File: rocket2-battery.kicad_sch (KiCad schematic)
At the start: 1 part

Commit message: Basic schematic
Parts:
- added C1: 1uF, symbol Device:C_Small
- added C2: 10uF, symbol Device:C_Small
- added C3: 0.1uF, symbol Device:C_Small
- added D1: BLUE_LED, symbol Device:LED_Small
- added D2: RED_LED, symbol Device:LED_Small
- added JP1: NO_Jump, symbol Jumper:Jumper_2_Open
- added Q1: DMG6968UDM-7, Package_TO_SOT_SMD:SOT-23-6, symbol Transistor_FET:DMG9926UDM
- added R1: 10k, symbol Device:R_Small
- added R2, R3, R9: 330, symbol Device:R_Small
- added R4: 27k, symbol Device:R_Small
- added R5: 375, symbol Device:R_Small
- added R6, R7: 100, symbol Device:R_Small
- added R8: 2.2k, symbol Device:R_Small
- added U2: BQ2970, Package_SON:WSON-6_1.5x1.5mm_P0.5mm, symbol Battery_Management:BQ297xy
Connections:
- net +5V: now reaches U1.1 (IN)
- net +5V: now also C1.1, C2.1, R2.2, R3.1
- net at U1.2 (ISET): now also R5.1
- net at U1.3 (TS): now also JP1.2 (B), R1.1
- net GND: now reaches U1.4 (GND)
- net GND: now also U1.9 (GND), C1.2, C2.2, C3.2, JP1.1 (A), Q1.3 (S2), R1.2, R4.2, R5.2, R8.1, U2.4 (VSS)
- net at U1.5 (STATUS): now also D1.1 (K)
- net at U1.6 (~{PG}): now also D2.1 (K)
- net at U1.7 (VSET): now also R4.1
- net BAT+: now reaches U1.8 (OUT)
- net BAT+: now also R9.1
- new net: Q1.2 (S1/D2), Q1.5 (S1/D2)
- new net: Q1.4 (G2), R6.1
- new net: Q1.6 (G1), R7.1
- new net: R7.2, U2.3 (Dout)
- new net: D2.2 (A), R2.1
- new net: R6.2, U2.2 (Cout)
- new net: D1.2 (A), R3.2
- new net: C3.1, R9.2, U2.5 (BAT)
- new net: R8.2, U2.6 (V-)
- new net BAT-: Q1.1 (D1)
- no-connect marks 0 -> 1
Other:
- note added: "DNP"

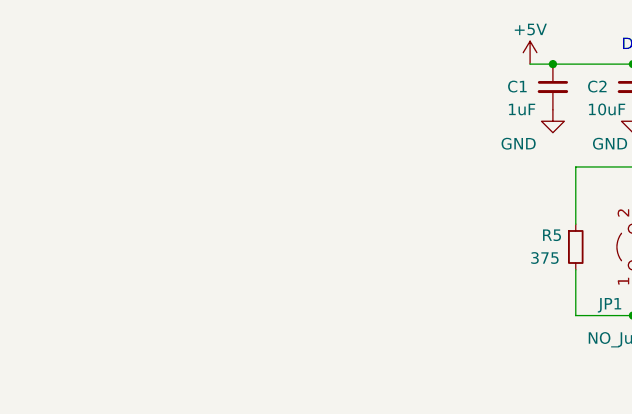
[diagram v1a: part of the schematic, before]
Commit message: added isolated 5v
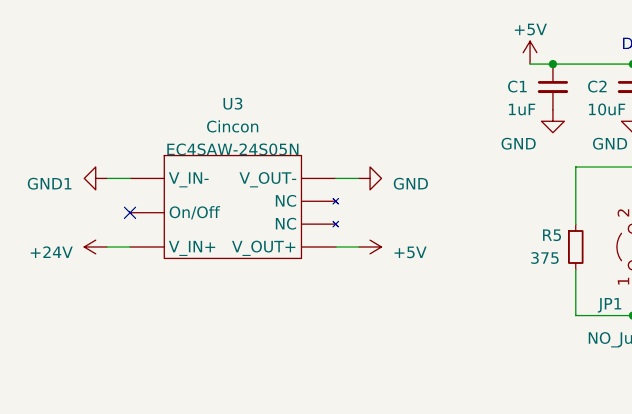
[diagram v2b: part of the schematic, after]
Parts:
- added U3: ~, symbol UCIRP-KiCAD-Lib:EC4SAW
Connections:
- net +5V: now also U3.6 (V_OUT+)
- net GND: now also U3.7 (V_OUT-)
- new net +24V: U3.2 (V_IN+)
- new net GND1: U3.1 (V_IN-)
- no-connect marks 1 -> 2
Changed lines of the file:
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@@
   )
   (no_connect (at 179.07 106.68))
+  (no_connect (at 54.61 92.71))
   (wire (pts (xy 200.66 80.01) (xy 205.74 80.01))
     (stroke (width 0) (type default))
@@
     (stroke (width 0) (type default))
   )
+  (wire (pts (xy 52.07 96.52) (xy 54.61 96.52))
+    (stroke (width 0) (type default))
+  )
   (wire (pts (xy 210.82 90.17) (xy 213.36 90.17))
     (stroke (width 0) (type default))
@@
     (stroke (width 0) (type default))
   )
+  (wire (pts (xy 52.07 88.9) (xy 54.61 88.9))
+    (stroke (width 0) (type default))
+  )
   (wire (pts (xy 130.81 104.14) (xy 165.1 104.14))
     (stroke (width 0) (type default))
@@
     (stroke (width 0) (type default))
   )
+  (wire (pts (xy 77.47 88.9) (xy 80.01 88.9))
+    (stroke (width 0) (type default))
+  )
   (wire (pts (xy 165.1 87.63) (xy 165.1 93.98))
     (stroke (width 0) (type default))
@@
   )
   (wire (pts (xy 213.36 80.01) (xy 213.36 90.17))
+    (stroke (width 0) (type default))
+  )
+  (wire (pts (xy 77.47 96.52) (xy 80.01 96.52))
     (stroke (width 0) (type default))
   )
@@
     )
   )
+  (symbol (lib_id "UCIRP-KiCAD-Lib:EC4SAW") (at 66.04 92.075 0) (unit 1)
+    (in_bom yes) (on_board yes) (dnp no) (fields_autoplaced)
+    (property "Reference" "U3" (at 66.04 80.645 0)
+      (effects (font (size 1.27 1.27)))
+    )
+    (property "Value" "~" (at 66.04 92.71 0)
+      (effects (font (size 1.27 1.27)))
+    )
+    (property "Footprint" "" (at 66.04 92.71 0)
+      (effects (font (size 1.27 1.27)) hide)
+    )
+    (property "Datasheet" "https://www.cincon.com/productdownload/Datasheet-EC4SAW-series.pdf" (at 66.04 92.71 0)
+      (effects (font (size 1.27 1.27)) hide)
+    )
+    (property "Manufacturer" "Cincon" (at 66.04 83.185 0)
+      (effects (font (size 1.27 1.27)))
+    )
+    (property "Part #" "EC4SAW-24S05N" (at 66.04 85.725 0)
+      (effects (font (size 1.27 1.27)))
+    )
+    (pin "1")
+    (pin "2")
+    (pin "3")
+    (pin "5")
+    (pin "6")
+    (pin "7")
+    (pin "8")
+    (instances
+      (project "rocket2-battery"
+        (path "/453543af-7e3c-49a0-a644-4bd49c4f86f8"
+          (reference "U3") (unit 1)
+        )
+      )
+    )
+  )
   (symbol (lib_id "Device:LED_Small") (at 147.32 95.25 270) (unit 1)
     (in_bom yes) (on_board yes) (dnp no)
@@
         (path "/453543af-7e3c-49a0-a644-4bd49c4f86f8"
           (reference "R6") (unit 1)
+        )
+      )
+    )
+  )
+  (symbol (lib_id "power:GND") (at 80.01 88.9 90) (unit 1)
+    (in_bom yes) (on_board yes) (dnp no) (fields_autoplaced)
+    (property "Reference" "#PWR010" (at 86.36 88.9 0)
+      (effects (font (size 1.27 1.27)) hide)
+    )
+    (property "Value" "GND" (at 83.82 89.535 90)
+      (effects (font (size 1.27 1.27)) (justify right))
+    )
+    (property "Footprint" "" (at 80.01 88.9 0)
+      (effects (font (size 1.27 1.27)) hide)
+    )
+    (property "Datasheet" "" (at 80.01 88.9 0)
+      (effects (font (size 1.27 1.27)) hide)
+    )
+    (pin "1")
+    (instances
+      (project "rocket2-battery"
+        (path "/453543af-7e3c-49a0-a644-4bd49c4f86f8"
+          (reference "#PWR010") (unit 1)
         )
       )
@@
     )
   )
+  (symbol (lib_id "power:+24V") (at 52.07 96.52 90) (unit 1)
+    (in_bom yes) (on_board yes) (dnp no) (fields_autoplaced)
+    (property "Reference" "#PWR011" (at 55.88 96.52 0)
+      (effects (font (size 1.27 1.27)) hide)
+    )
+    (property "Value" "+24V" (at 48.26 97.155 90)
+      (effects (font (size 1.27 1.27)) (justify left))
+    )
+    (property "Footprint" "" (at 52.07 96.52 0)
+      (effects (font (size 1.27 1.27)) hide)
+    )
+    (property "Datasheet" "" (at 52.07 96.52 0)
+      (effects (font (size 1.27 1.27)) hide)
+    )
+    (pin "1")
+    (instances
+      (project "rocket2-battery"
+        (path "/453543af-7e3c-49a0-a644-4bd49c4f86f8"
+          (reference "#PWR011") (unit 1)
+        )
+      )
+    )
+  )
   (symbol (lib_id "Device:R_Small") (at 139.7 100.33 90) (unit 1)
     (in_bom yes) (on_board yes) (dnp no)
@@
     )
   )
+  (symbol (lib_id "power:+5V") (at 80.01 96.52 270) (unit 1)
+    (in_bom yes) (on_board yes) (dnp no) (fields_autoplaced)
+    (property "Reference" "#PWR09" (at 76.2 96.52 0)
+      (effects (font (size 1.27 1.27)) hide)
+    )
+    (property "Value" "+5V" (at 83.82 97.155 90)
+      (effects (font (size 1.27 1.27)) (justify left))
+    )
+    (property "Footprint" "" (at 80.01 96.52 0)
+      (effects (font (size 1.27 1.27)) hide)
+    )
+    (property "Datasheet" "" (at 80.01 96.52 0)
+      (effects (font (size 1.27 1.27)) hide)
+    )
+    (pin "1")
+    (instances
+      (project "rocket2-battery"
+        (path "/453543af-7e3c-49a0-a644-4bd49c4f86f8"
+          (reference "#PWR09") (unit 1)
+        )
+      )
+    )
+  )
   (symbol (lib_id "Device:C_Small") (at 110.49 78.74 0) (unit 1)
     (in_bom yes) (on_board yes) (dnp no)
@@
         )
       )
+    )
+  )
+  (symbol (lib_id "power:GND1") (at 52.07 88.9 270) (unit 1)
+    (in_bom yes) (on_board yes) (dnp no) (fields_autoplaced)
+    (property "Reference" "#PWR012" (at 45.72 88.9 0)
+      (effects (font (size 1.27 1.27)) hide)
+    )
+    (property "Value" "GND1" (at 48.26 89.535 90)
+      (effects (font (size 1.27 1.27)) (justify right))
+    )
+    (property "Footprint" "" (at 52.07 88.9 0)
+      (effects (font (size 1.27 1.27)) hide)
+    )
+    (property "Datasheet" "" (at 52.07 88.9 0)
+      (effects (font (size 1.27 1.27)) hide)
+    )
+    (pin "1")
+    (instances
+      (project "rocket2-battery"
+        (path "/453543af-7e3c-49a0-a644-4bd49c4f86f8"
+          (reference "#PWR012") (unit 1)
+        )
+      )

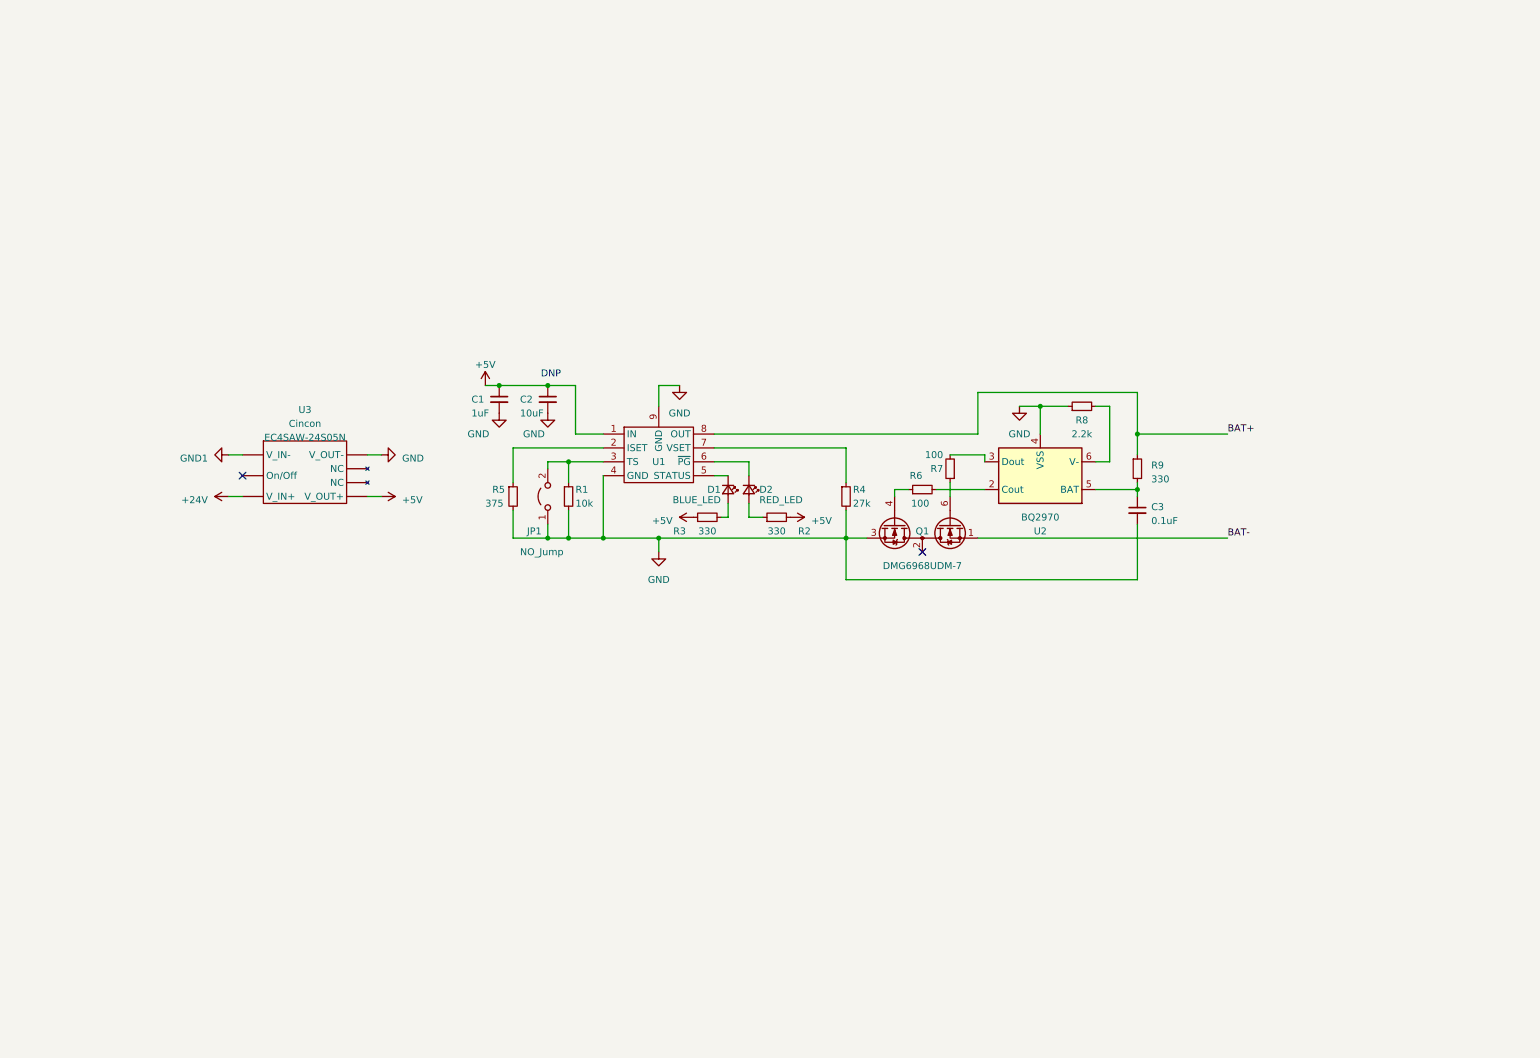
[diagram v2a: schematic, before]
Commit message: turned into heirarchical
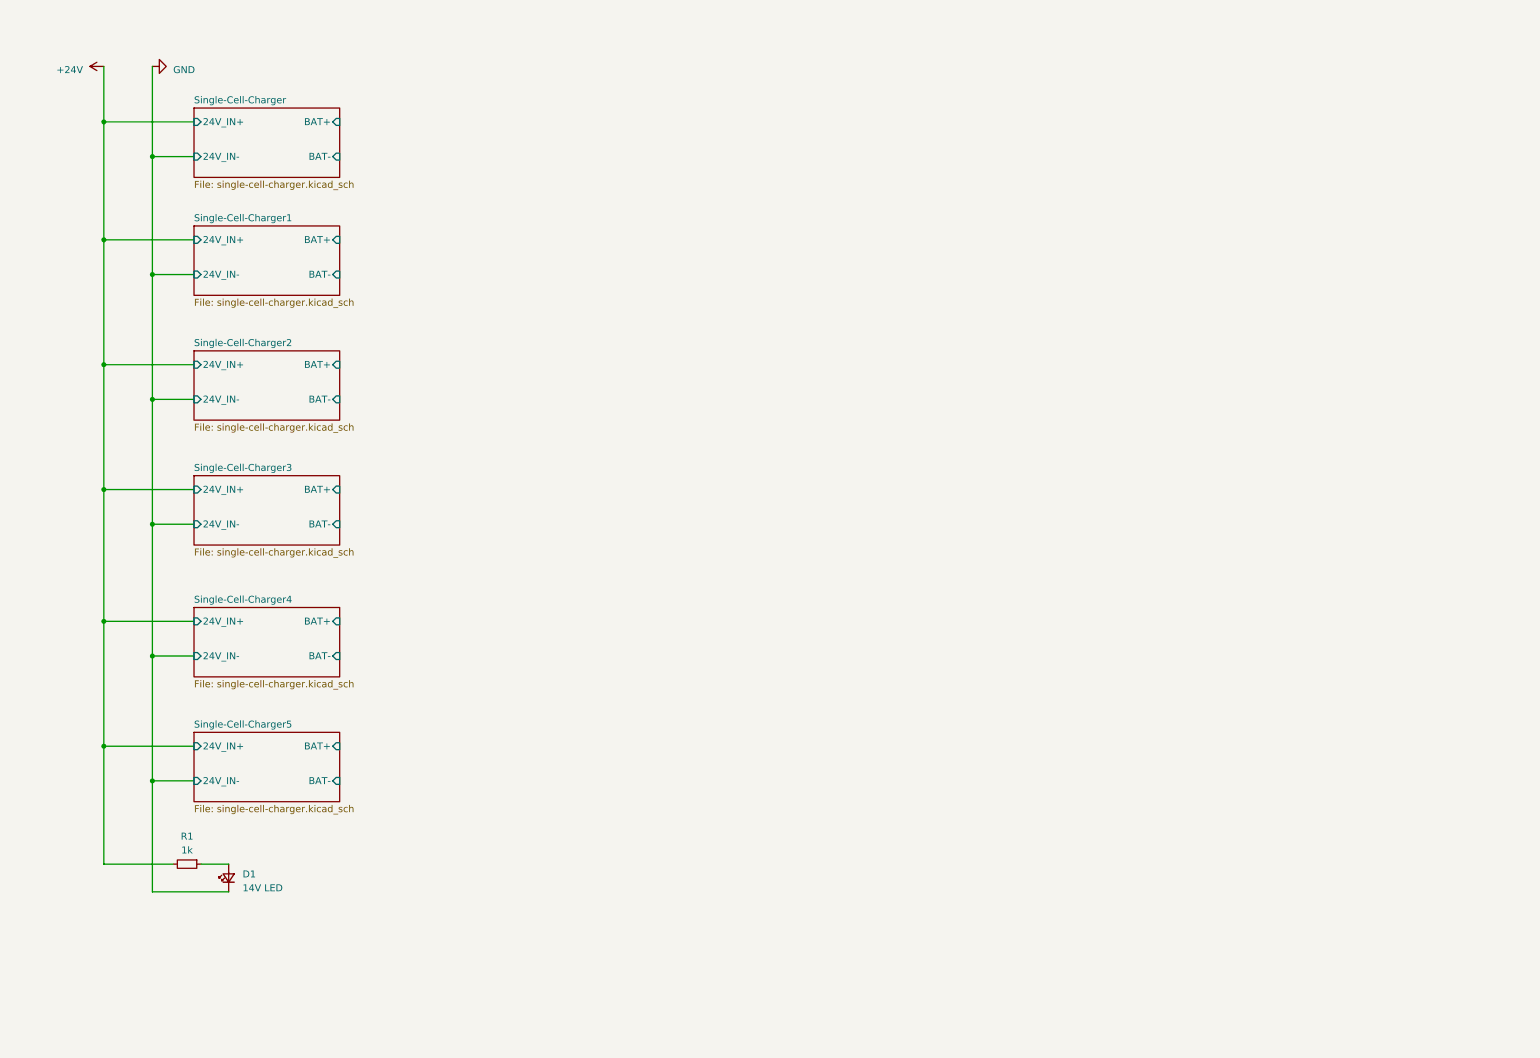
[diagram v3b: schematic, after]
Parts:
- removed C1: 1uF, symbol Device:C_Small
- removed C2: 10uF, symbol Device:C_Small
- removed C3: 0.1uF, symbol Device:C_Small
- removed D2: RED_LED, symbol Device:LED_Small
- removed JP1: NO_Jump, symbol Jumper:Jumper_2_Open
- removed Q1: DMG6968UDM-7, Package_TO_SOT_SMD:SOT-23-6, symbol Transistor_FET:DMG9926UDM
- removed R2, R3, R9: 330, symbol Device:R_Small
- removed R4: 27k, symbol Device:R_Small
- removed R5: 375, symbol Device:R_Small
- removed R6, R7: 100, symbol Device:R_Small
- removed R8: 2.2k, symbol Device:R_Small
- removed U1: ~, Package_SON:WSON-8-1EP_2x2mm_P0.5mm_EP0.9x1.6mm_ThermalVias, symbol UCIRP-KiCAD-Lib:BQ25170
- removed U2: BQ2970, Package_SON:WSON-6_1.5x1.5mm_P0.5mm, symbol Battery_Management:BQ297xy
- removed U3: ~, symbol UCIRP-KiCAD-Lib:EC4SAW
- D1: value BLUE_LED -> 14V LED; footprint (none) -> LED_THT:LED_D5.0mm
- R1: value 10k -> 1k
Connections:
- net +24V: now also R1.2
- net GND: now also D1.1 (K); no longer R1.2
- net at R1.1: now also D1.2 (A)
- no-connect marks 2 -> 0
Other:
- added sheet Single-Cell-Charger (single-cell-charger.kicad_sch)
- added sheet Single-Cell-Charger1 (single-cell-charger.kicad_sch)
- added sheet Single-Cell-Charger2 (single-cell-charger.kicad_sch)
- added sheet Single-Cell-Charger3 (single-cell-charger.kicad_sch)
- added sheet Single-Cell-Charger4 (single-cell-charger.kicad_sch)
- added sheet Single-Cell-Charger5 (single-cell-charger.kicad_sch)
- note removed: "DNP"

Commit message: finished schematic; (major parts selected)
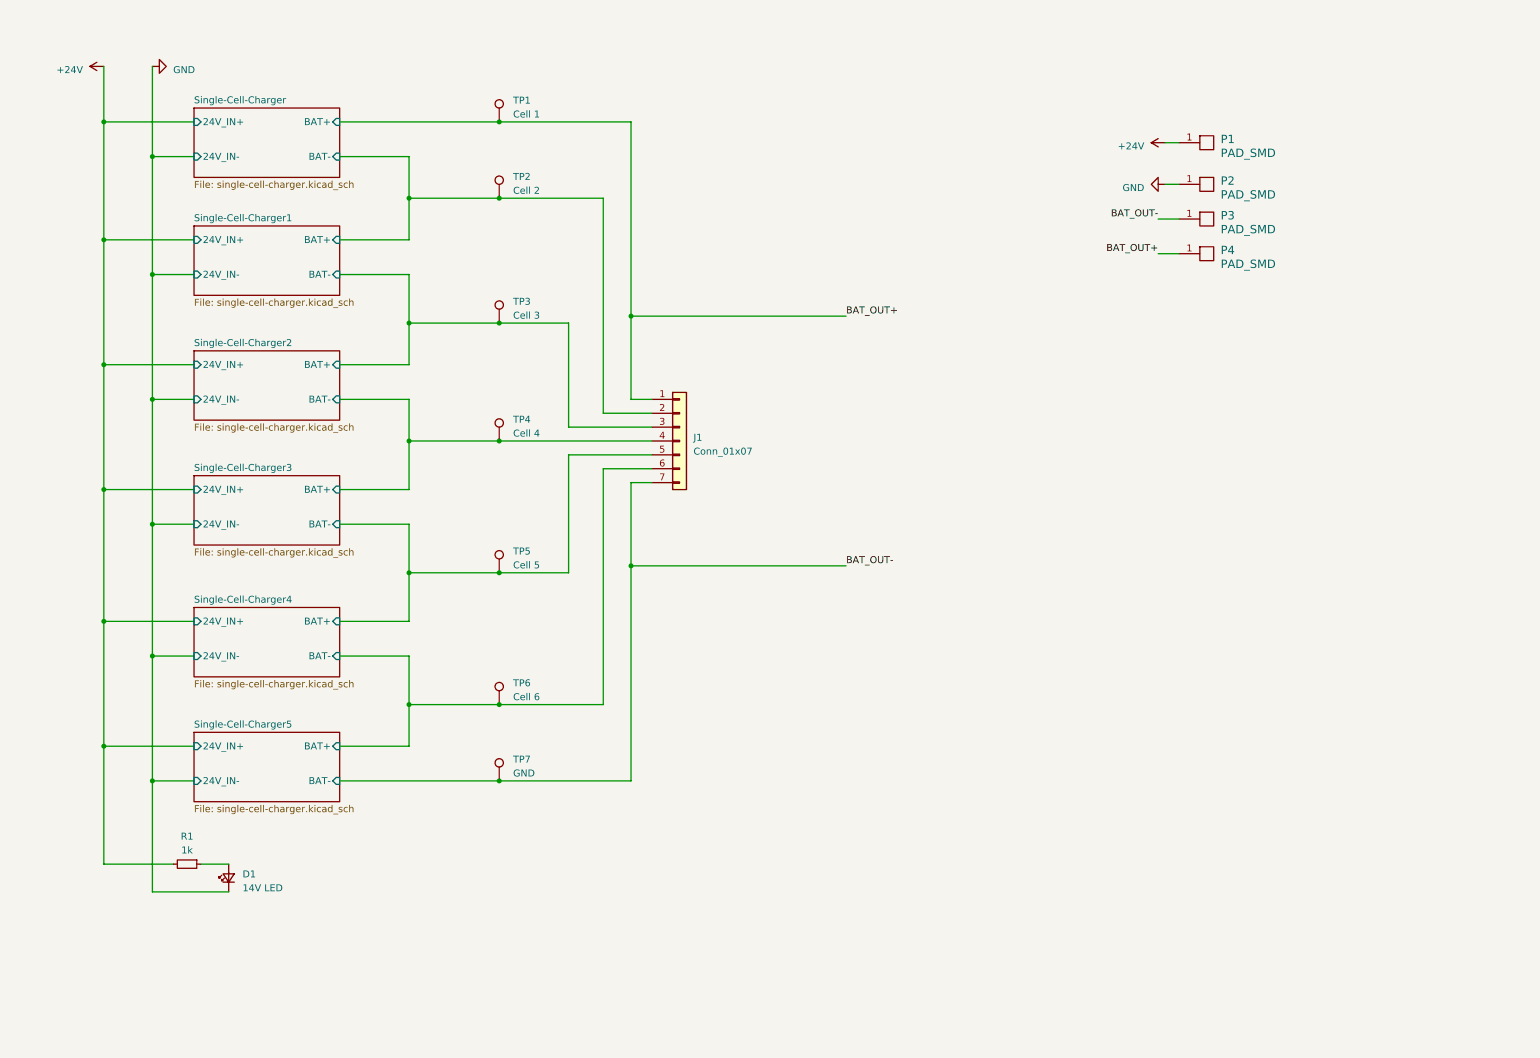
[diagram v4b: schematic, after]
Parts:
- added J1: Conn_01x07, Connector_JST:JST_PH_B7B-PH-K_1x07_P2.00mm_Vertical, symbol Connector_Generic:Conn_01x07
- added P1, P2, P3, P4: PAD_SMD, symbol pkl_misc:PAD_SMD
- added TP1: Cell 1, symbol Connector:TestPoint
- added TP2: Cell 2, symbol Connector:TestPoint
- added TP3: Cell 3, symbol Connector:TestPoint
- added TP4: Cell 4, symbol Connector:TestPoint
- added TP5: Cell 5, symbol Connector:TestPoint
- added TP6: Cell 6, symbol Connector:TestPoint
- added TP7: GND, symbol Connector:TestPoint
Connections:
- net +24V: now also P1.1 (PAD)
- net GND: now also P2.1 (PAD)
- net Single-Cell-Charger/BAT-: now also J1.2 (Pin_2), TP2.1
- net Single-Cell-Charger1/BAT-: now also J1.3 (Pin_3), TP3.1
- net Single-Cell-Charger2/BAT-: now also J1.4 (Pin_4), TP4.1
- net Single-Cell-Charger3/BAT-: now also J1.5 (Pin_5), TP5.1
- net Single-Cell-Charger4/BAT-: now also J1.6 (Pin_6), TP6.1
- new net BAT_OUT+: J1.1 (Pin_1), P4.1 (PAD), TP1.1
- new net BAT_OUT-: J1.7 (Pin_7), P3.1 (PAD), TP7.1
